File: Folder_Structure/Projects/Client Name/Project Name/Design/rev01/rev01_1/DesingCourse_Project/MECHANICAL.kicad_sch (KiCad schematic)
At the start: 0 parts

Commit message: Update 6
SCH and LIB for MOSFET page done, missing passive components
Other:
- company: (none) -> Integro Consulting AB
- title: (none) -> PCB Mastery Project
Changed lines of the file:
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@@
 	(generator_version "9.0")
 	(paper "A4")
+	(title_block
+		(title "PCB Mastery Project")
+		(date "2026-01-27")
+		(rev "001")
+		(company "Integro Consulting AB")
+		(comment 1 "TBD")
+		(comment 2 "TBD")
+		(comment 3 "TBD")
+		(comment 4 "Josue Godinez")
+	)
 )

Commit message: Update 12
Until STEP-DOWN page, all components have complete libraries.

Creation and incluison of all logos and labels libraries
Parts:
- added FID1, FID2, FID3: 1mm/circular, Fiducial:Fiducial_1mm_Mask2mm, symbol Mechanical:Fiducial
- added ID1: ~, JGB_Library:hot-surface, symbol JGB_Library:Hot_Surface_logo
- added ID2: ~, JGB_Library:high-voltage, symbol JGB_Library:High_Voltage_logo
- added ID3: ~, JGB_Library:ESD-suceptible, symbol JGB_Library:DNT_logo
- added ID4: ~, JGB_Library:IC-logo, symbol JGB_Library:Integro_logo
- added ID5: ~, JGB_Library:4_Layer_ID, symbol JGB_Library:4LAYER_ID
- added ID6: ~, JGB_Library:Project_ID, symbol JGB_Library:PROJECT_ID_CODE_REV_&_NAME
- added MH1, MH2, MH3, MH4: M4.5, MountingHole:MountingHole_4.5mm_Pad_Via, symbol Mechanical:MountingHole_Pad_MP
- added R60, R61, R62, R63: 0R, Resistor_SMD:R_0603_1608Metric, symbol Device:R
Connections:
- new net: MH4.MP, R63.1
- new net: MH1.MP, R60.1
- new net: MH3.MP, R62.1
- new net: MH2.MP, R61.1
- new net GND: R60.2, R61.2, R62.2, R63.2
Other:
- note added: "L1"
- note added: "L2"
- note added: "L3"
- note added: "L4"
- note added: "LOGOS & LABELS"
- note added: "MECHANICAL"
- note added: "MOUNTING HOLES & FIDUCIAL"

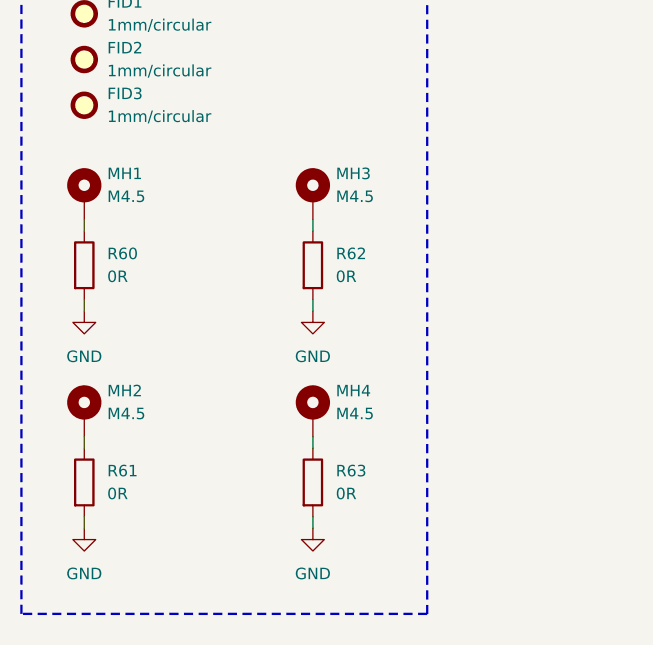
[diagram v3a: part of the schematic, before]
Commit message: Update 16
Initial component placement done
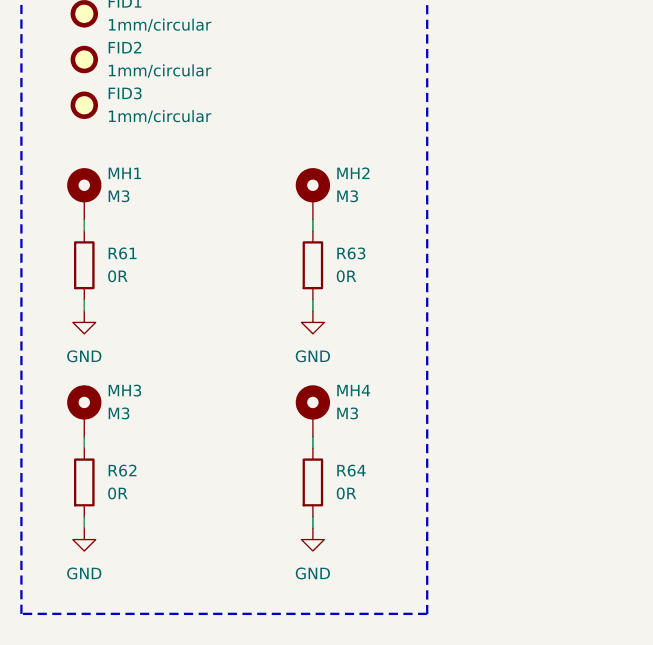
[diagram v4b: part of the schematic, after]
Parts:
- MH1, MH2, MH3, MH4: value M4.5 -> M3; footprint MountingHole:MountingHole_4.5mm_Pad_Via -> MountingHole:MountingHole_3mm_Pad_Via
- renumbered R60 to R61, R61 to R62, R62 to R63, R63 to R64
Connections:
- net at R64.1: now also MH4.1; no longer MH4.MP
- net at R61.1: now also MH1.1; no longer MH1.MP
- net at R63.1: now also MH2.1; no longer MH3.MP
- net at R62.1: now also MH3.1; no longer MH2.MP

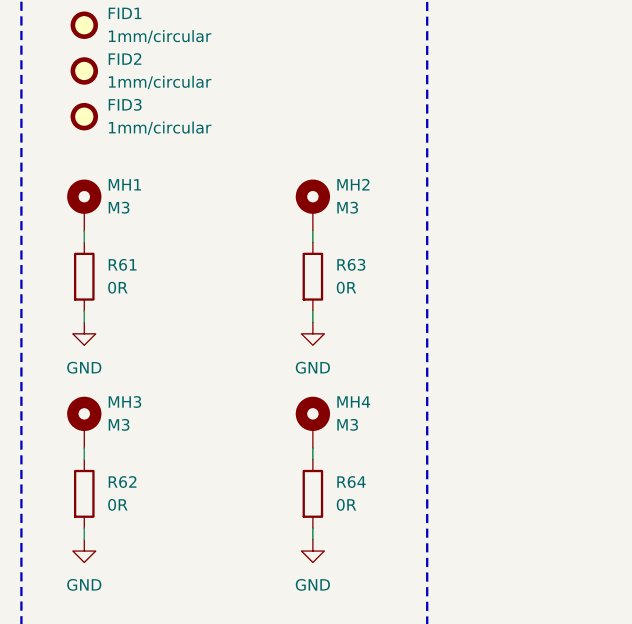
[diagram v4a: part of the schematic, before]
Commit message: Update17
Design rules and stack defined.

Check againg DR and proceed with layout.
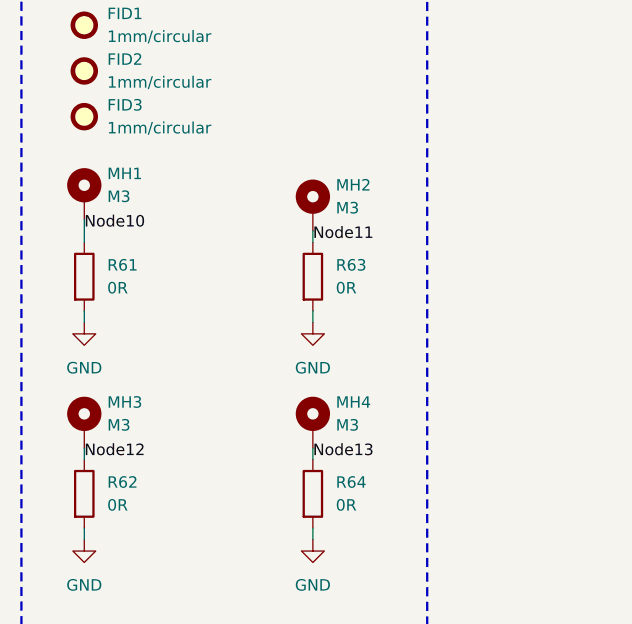
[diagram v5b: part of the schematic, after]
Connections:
- net Node10: now reaches MH1.1, R61.1
- net Node12: now reaches MH3.1, R62.1
- net Node13: now reaches MH4.1, R64.1
- net Node11: now reaches MH2.1, R63.1
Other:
- moved on the sheet: MH1
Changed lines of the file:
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@@
 	(wire
 		(pts
-			(xy 24.13 73.66) (xy 24.13 72.39)
+			(xy 24.13 73.66) (xy 24.13 71.12)
 		)
 		(stroke
@@
 			(width 0)
 			(type default)
+		)
+	)
+	(label "Node11"
+		(at 49.53 73.66 0)
+		(effects
+			(font
+				(size 1.27 1.27)
+			)
+			(justify left bottom)
+		)
+	)
+	(label "Node12"
+		(at 24.13 97.79 0)
+		(effects
+			(font
+				(size 1.27 1.27)
+			)
+			(justify left bottom)
+		)
+	)
+	(label "Node10"
+		(at 24.13 72.39 0)
+		(effects
+			(font
+				(size 1.27 1.27)
+			)
+			(justify left bottom)
+		)
+	)
+	(label "Node13"
+		(at 49.53 97.79 0)
+		(effects
+			(font
+				(size 1.27 1.27)
+			)
+			(justify left bottom)
 		)
 	)
@@
 		(lib_name "MountingHole_Pad_MP_1")
 		(lib_id "Mechanical:MountingHole_Pad_MP")
-		(at 24.13 69.85 0)
+		(at 24.13 68.58 0)
 		(unit 1)
 		(exclude_from_sim no)
@@
 		(fields_autoplaced yes)
 		(property "Reference" "MH1"
-			(at 26.67 67.3099 0)
+			(at 26.67 66.0399 0)
 			(effects
 				(font
@@
 		)
 		(property "Value" "M3"
-			(at 26.67 69.8499 0)
+			(at 26.67 68.5799 0)
 			(effects
 				(font
@@
 		)
 		(property "Footprint" "MountingHole:MountingHole_3mm_Pad_Via"
-			(at 24.13 69.85 0)
+			(at 24.13 68.58 0)
 			(effects
 				(font
@@
 		)
 		(property "Datasheet" "~"
-			(at 24.13 69.85 0)
+			(at 24.13 68.58 0)
 			(effects
 				(font
@@
 		)
 		(property "Description" "Mounting Hole for a 3mm screw"
-			(at 24.13 69.85 0)
+			(at 24.13 68.58 0)
 			(effects
 				(font
@@
 		)
 		(property "MNP" ""
-			(at 24.13 69.85 0)
+			(at 24.13 68.58 0)
 			(effects
 				(font
@@
 		)
 		(property "MF" ""
-			(at 24.13 69.85 0)
-			(effects
-				(font
+			(at 24.13 68.58 0)
+			(effects
+				(font

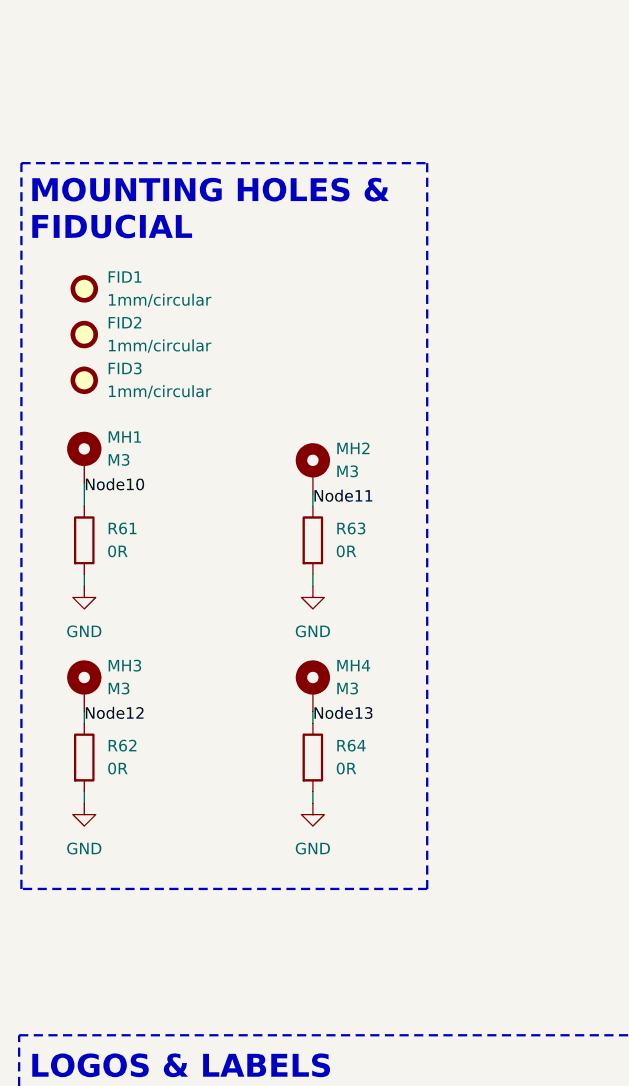
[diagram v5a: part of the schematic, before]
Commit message: Update18
Layout finished, clean up or layout and designators.
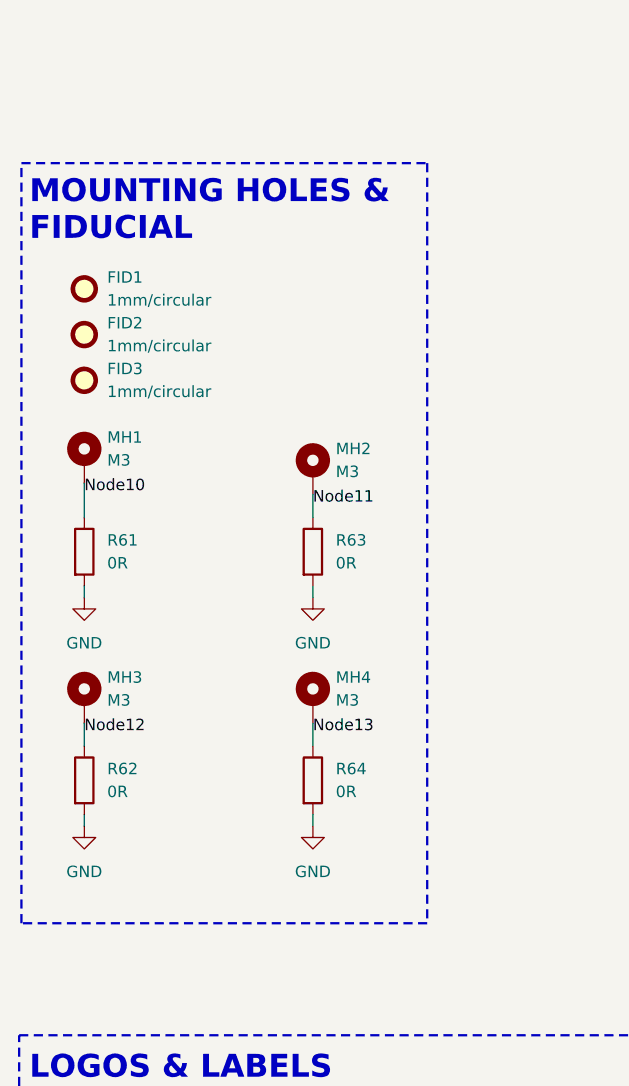
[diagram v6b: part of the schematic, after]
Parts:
- removed MH1, MH2, MH3, MH4: M3, MountingHole:MountingHole_3mm_Pad_Via, symbol Mechanical:MountingHole_Pad_MP
- added MH1, MH2, MH3, MH4: M3, MountingHole:MountingHole_3mm_Pad_Via, symbol Mechanical:MountingHole_Pad
- ID5: now in the parts list
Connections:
- net Node10: now also MH1.1
- net Node11: now also MH2.1
- net Node12: now also MH3.1
- net Node13: now also MH4.1
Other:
- moved on the sheet: R61, R62, R63, R64
